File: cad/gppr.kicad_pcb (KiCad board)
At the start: 2 copper layers, 48 x 85 mm, 32 parts, among them J1 Conn_01x04_Female, J2 Conn_01x02_Female, J3 Conn_Coaxial, Q1 IRLR2908, U1 TPS7A470X

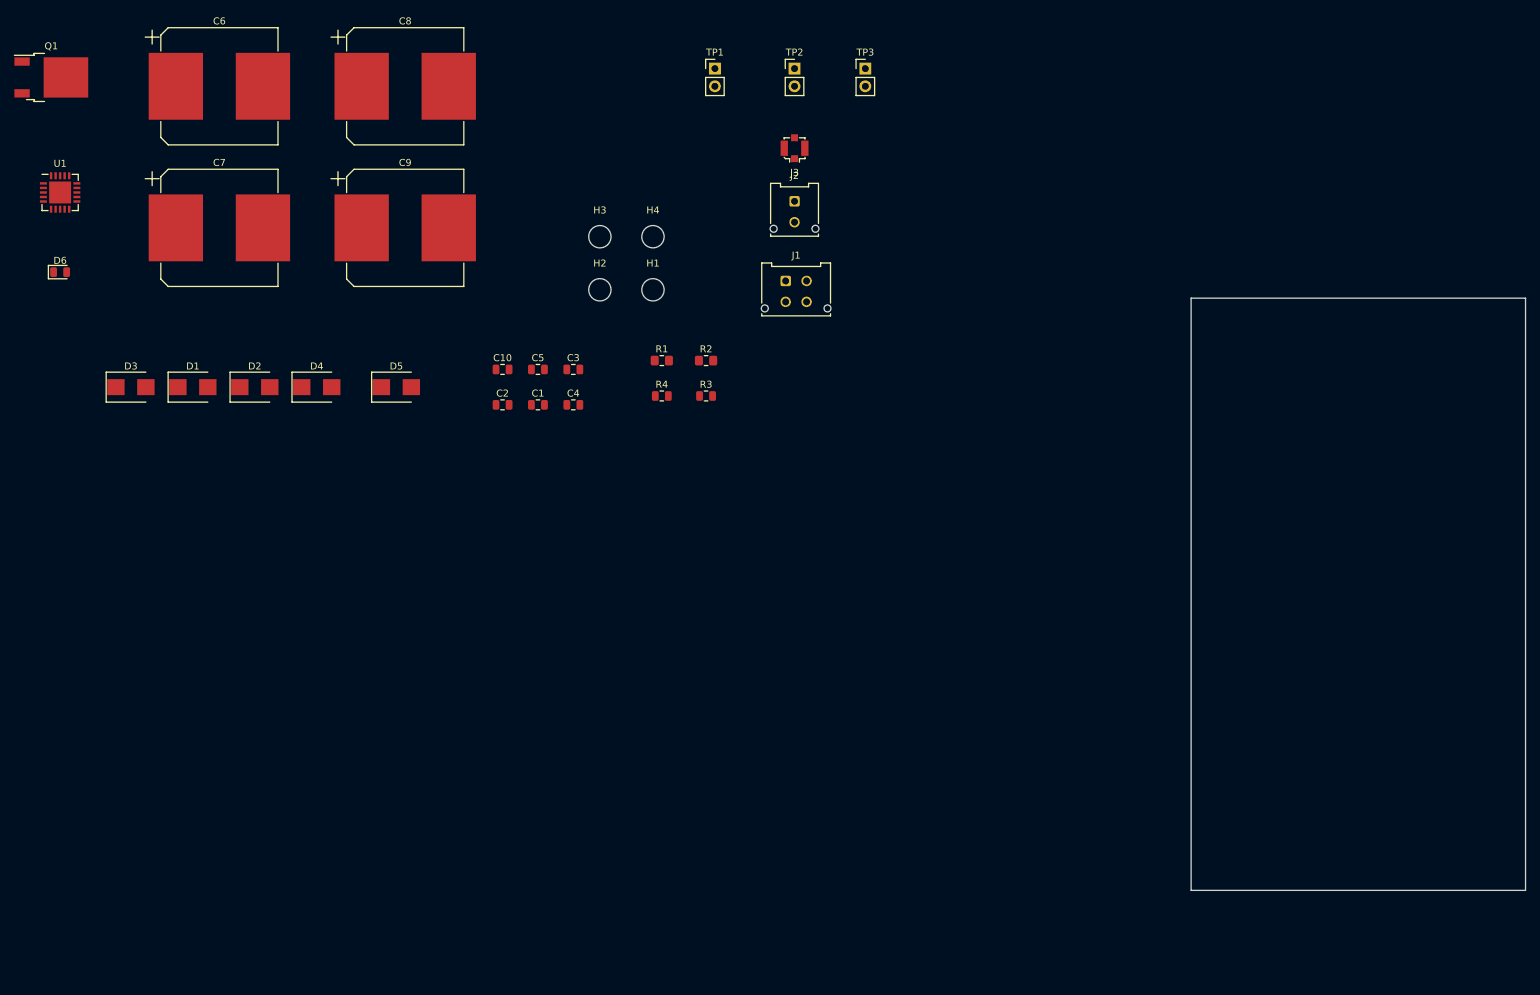
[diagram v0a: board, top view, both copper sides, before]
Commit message: basic component placement, prep for trace routing
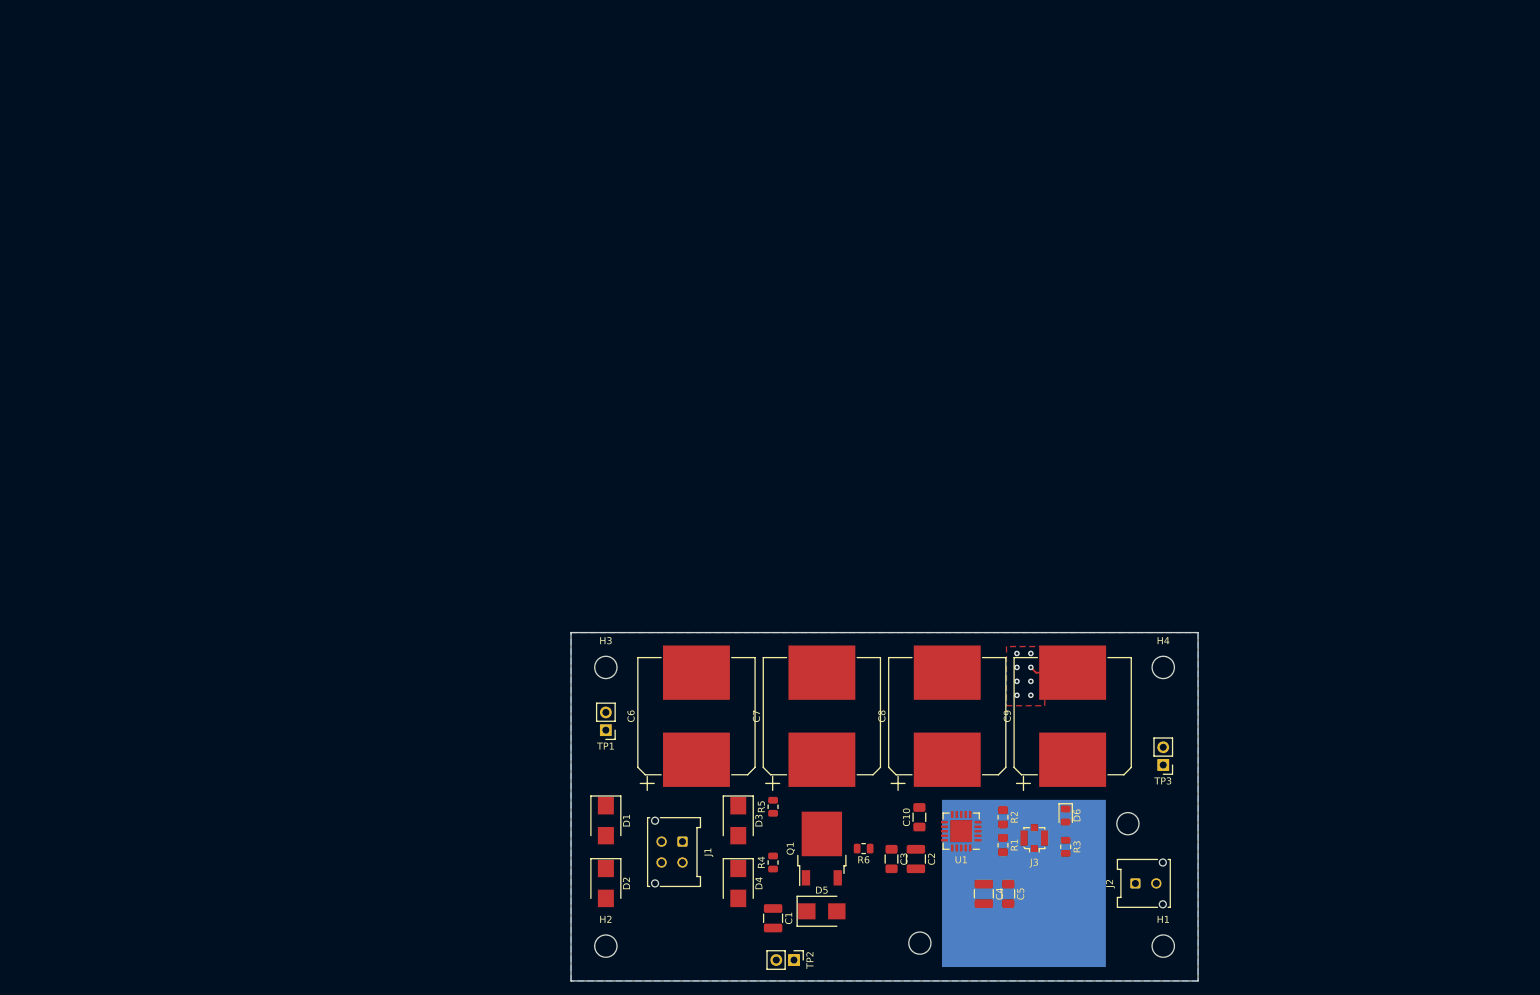
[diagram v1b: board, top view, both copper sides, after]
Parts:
- added HS1: Heatsink_Pad, Heatsink:Heatsink_960-23-XX-F-AB-0, F.Cu at (165.0, 136.0)
- added R5: 0Ω, Resistor_SMD:R_0805_2012Metric, F.Cu at (129.0, 125.0)
- added R6: 0Ω, Resistor_SMD:R_0805_2012Metric, F.Cu at (142.0, 131.0)
- C1, C2, C4: footprint Capacitor_SMD:C_0805_2012Metric -> Capacitor_SMD:C_1210_3225Metric
- C10, C3, C5: footprint Capacitor_SMD:C_0805_2012Metric -> Capacitor_SMD:C_1206_3216Metric
- moved D6 164.1 mm to (171.0, 126.2), turned to 270 degrees
- moved U1 158.5 mm to (156.0, 128.5), turned to 180 degrees
- moved Q1 156.5 mm to (136.0, 131.0), turned to 90 degrees
- moved TP2 128.0 mm to (132.0, 147.0), turned to 270 degrees
- moved H1 119.3 mm to (185.0, 145.0)
- moved C8 119.3 mm to (154.0, 112.0), turned to 90 degrees
- moved C9 118.7 mm to (172.0, 112.0), turned to 90 degrees
- moved C6 113.4 mm to (118.0, 112.0), turned to 90 degrees
- moved C7 111.3 mm to (136.0, 112.0), turned to 90 degrees
- moved J2 109.4 mm to (181.0, 136.0), turned to 90 degrees
- moved TP3 108.7 mm to (185.0, 119.0), turned to 180 degrees
- moved D3 107.1 mm to (124.0, 127.0), turned to 270 degrees
- moved J3 104.8 mm to (166.5, 129.5)
- moved C5 101.1 mm to (162.8, 137.5), turned to 270 degrees
- moved D5 96.9 mm to (136.0, 140.0)
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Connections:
- D5 pad 2: Net-(C2-Pad1) -> Net-(D5-Pad2)
- Q1 pad 2: Net-(C6-Pad1) -> Net-(Q1-Pad2)
- Q1 pad 3: Net-(C2-Pad1) -> Net-(D5-Pad2)
- R4 pad 2: Net-(C6-Pad1) -> Net-(Q1-Pad2)
- TP2 pad 1: Net-(C2-Pad1) -> Net-(D5-Pad2)
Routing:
- net GND: track 0.00 -> 6.31 mm, vias 0 -> 8
- added copper zone on B.Cu, net GND
- added copper zone on F.Cu, net GND
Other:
- board size 48 x 85 mm -> 90 x 50 mm
- net class Default: trace_width 0.25 -> 0.35
- rule pad_to_mask_clearance: 0.051 -> 0

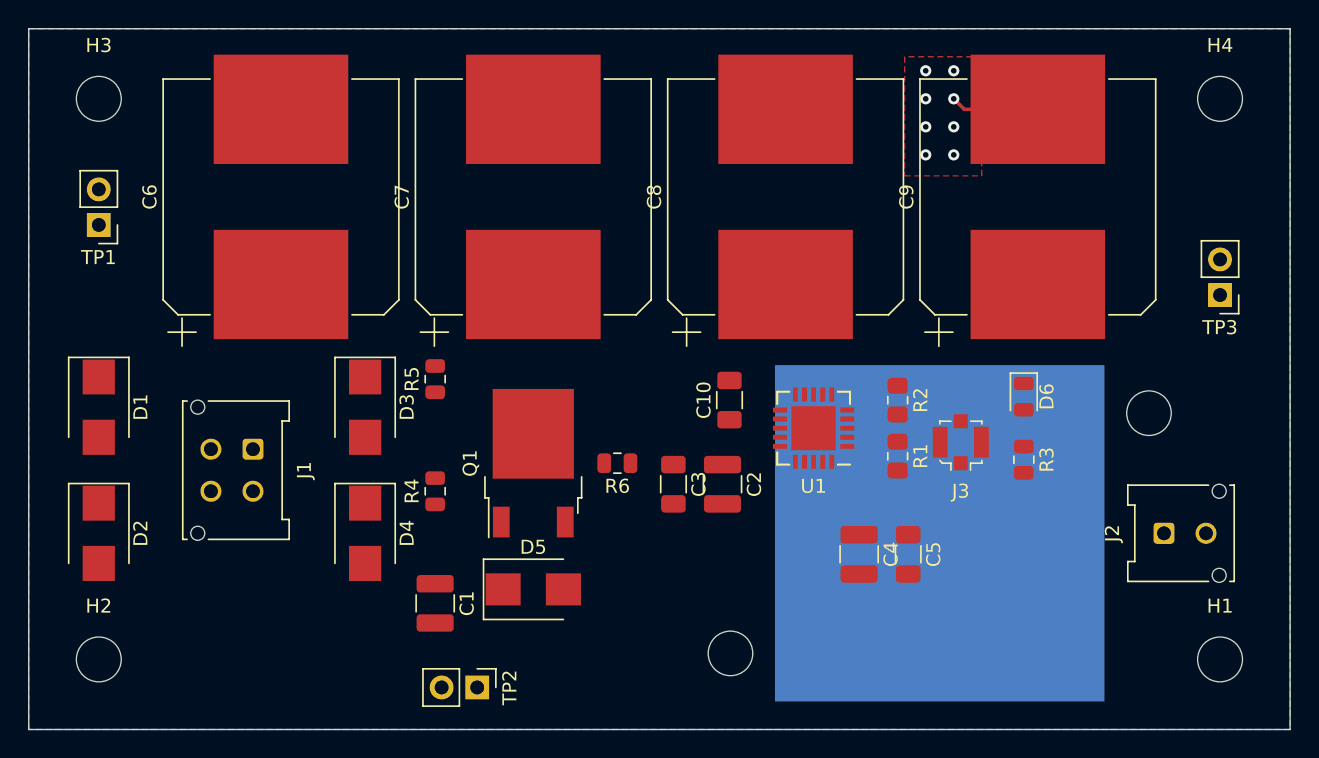
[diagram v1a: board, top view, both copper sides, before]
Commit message: change heatsink footprint from bottom to top side
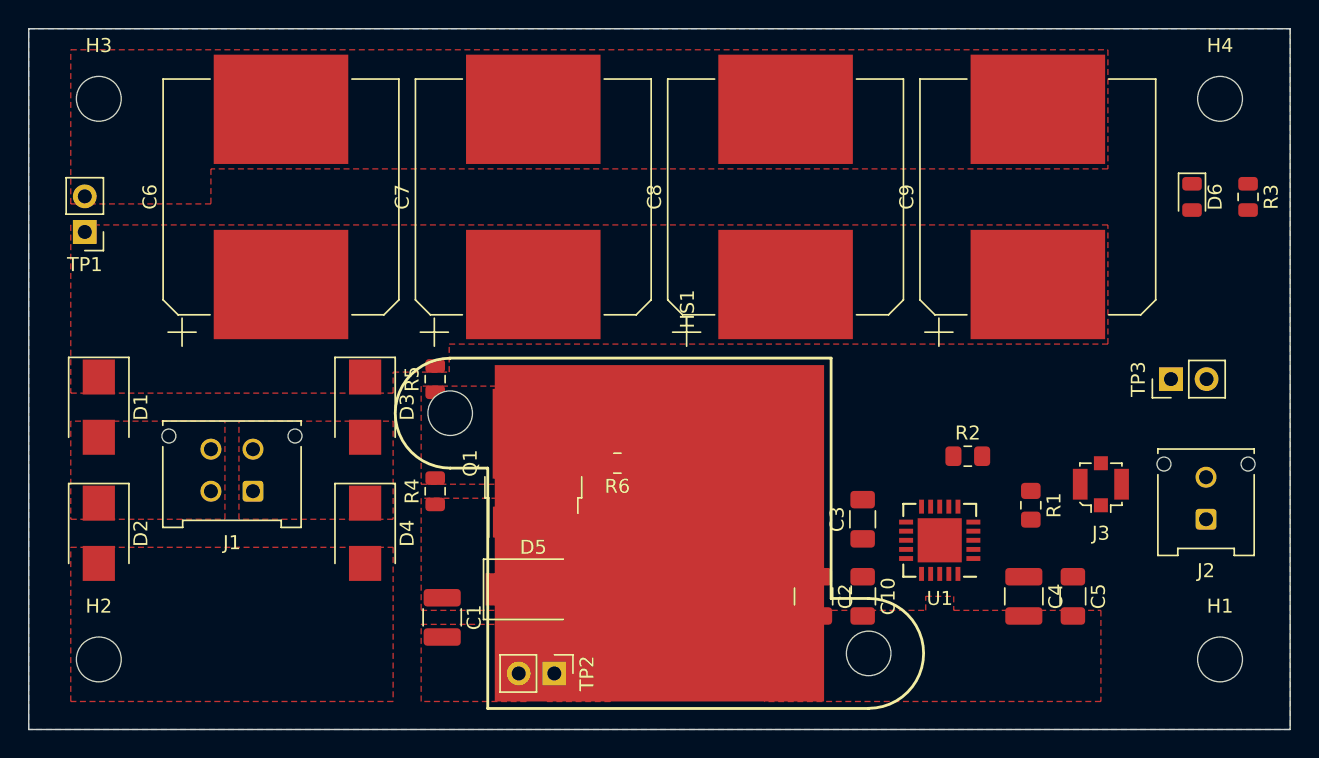
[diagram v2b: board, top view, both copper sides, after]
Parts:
- HS1: footprint Heatsink:Heatsink_960-23-XX-F-AB-0 -> Heatsink:Heatsink_960-23-XX-F-AB-0_Top
- moved R3 24.6 mm to (187.0, 112.0)
- moved HS1 20.0 mm to (145.0, 136.0)
- moved D6 18.6 mm to (183.0, 112.0)
- moved C10 16.9 mm to (159.5, 140.5), turned to 270 degrees
- moved C3 13.7 mm to (159.5, 135.0), turned to 90 degrees
- moved C4 12.1 mm to (171.0, 140.5)
- moved C5 12.1 mm to (174.5, 140.5)
- moved U1 12.0 mm to (165.0, 136.5)
- moved J3 10.4 mm to (176.5, 132.5)
- moved C2 10.3 mm to (156.0, 140.5)
- moved R1 10.1 mm to (171.5, 134.0)
- moved TP3 6.95 mm to (181.5, 125.0), turned to 90 degrees
- moved R2 6.40 mm to (167.0, 130.5), turned to 0 degrees
- moved TP2 5.59 mm to (137.5, 146.0)
- moved J2 3.16 mm to (184.0, 135.0), turned to 180 degrees
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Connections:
- U1 pad 17: Net-(U1-Pad17) -> GND
- U1 pad 18: Net-(U1-Pad18) -> GND
- U1 pad 19: Net-(U1-Pad19) -> GND
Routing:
- net GND: track 6.31 -> 0.00 mm, vias 8 -> 0
- added copper zone on F.Cu, net Net-(C1-Pad1)
- added copper zone on F.Cu, net Net-(C6-Pad1)
- added copper zone on F.Cu, net Net-(D1-Pad2)
- added copper zone on F.Cu, net Net-(D3-Pad2)
- added copper zone on F.Cu, net Net-(D5-Pad2)
- added copper zone on F.Cu, net Net-(Q1-Pad2)

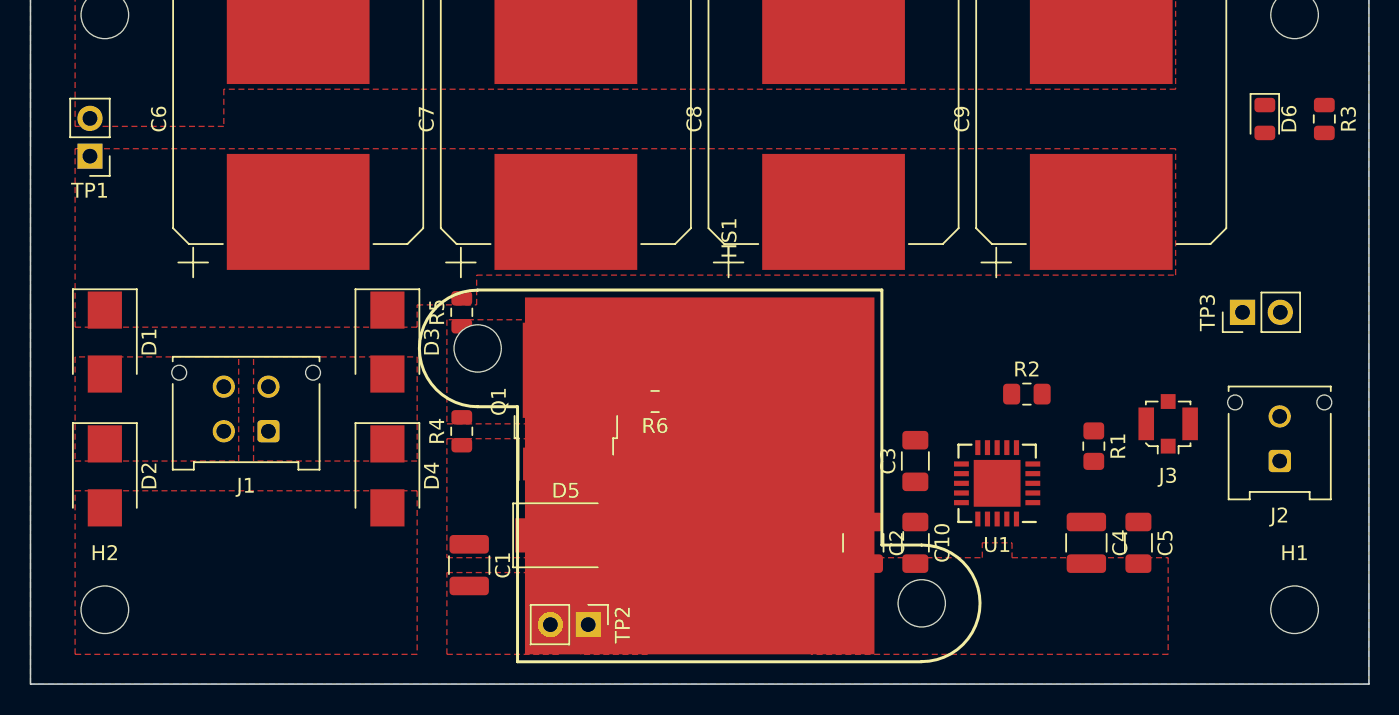
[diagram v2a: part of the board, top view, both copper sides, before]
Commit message: reposition components, prep to route
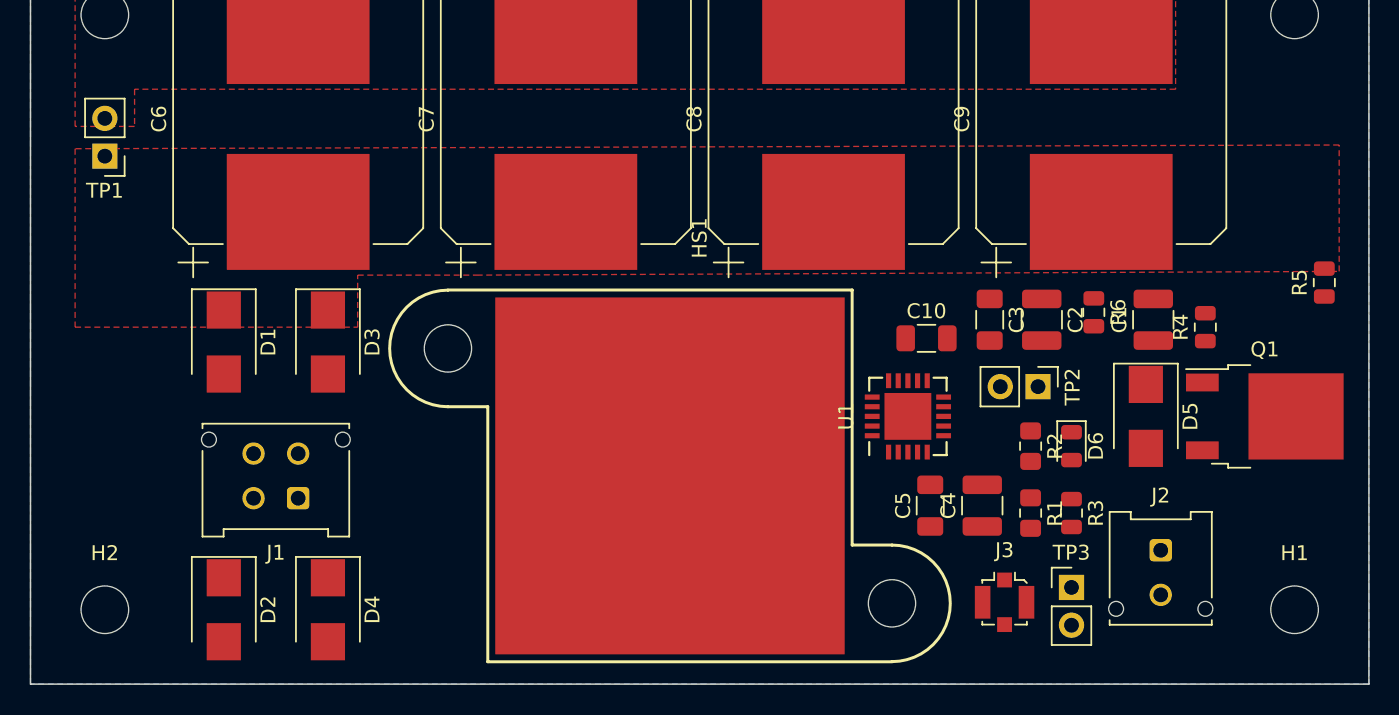
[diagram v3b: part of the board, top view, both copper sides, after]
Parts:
- moved R5 58.0 mm to (187.0, 123.0)
- moved R4 50.5 mm to (179.0, 126.0)
- moved C1 48.9 mm to (175.5, 125.5), turned to 90 degrees
- moved Q1 47.0 mm to (183.0, 132.0), turned to 0 degrees
- moved D5 39.8 mm to (175.0, 132.0), turned to 270 degrees
- moved TP2 34.2 mm to (167.8, 130.0)
- moved R3 31.5 mm to (170.0, 138.5)
- moved R6 30.1 mm to (171.5, 125.0), turned to 270 degrees
- moved D6 25.6 mm to (170.0, 134.0)
- moved TP3 21.8 mm to (170.0, 143.5), turned to 0 degrees
- moved C2 19.2 mm to (168.0, 125.5)
- moved J3 16.3 mm to (165.5, 144.5), turned to 180 degrees
- moved C5 14.2 mm to (160.5, 138.0), turned to 90 degrees
- moved C10 13.8 mm to (160.2, 126.8), turned to 0 degrees
- moved D2 12.0 mm to (113.0, 145.0)
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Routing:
- removed copper zone on F.Cu, net Net-(C1-Pad1)
- removed copper zone on F.Cu, net Net-(D1-Pad2)
- removed copper zone on F.Cu, net Net-(D3-Pad2)
- removed copper zone on F.Cu, net Net-(D5-Pad2)
- removed copper zone on F.Cu, net Net-(Q1-Pad2)

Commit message: route the board
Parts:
- moved TP1 79.5 mm to (184.5, 115.0)
- moved D3 17.0 mm to (108.0, 115.0)
- moved D1 15.3 mm to (103.5, 115.0)
- moved D4 15.0 mm to (108.0, 136.0)
- moved J1 14.1 mm to (108.0, 127.5)
- moved C2 13.8 mm to (154.5, 128.5), turned to 180 degrees
- moved D2 13.1 mm to (103.5, 136.0)
- moved R6 11.5 mm to (160.0, 125.0), turned to 0 degrees
- moved HS1 11.0 mm to (132.0, 136.0)
- moved C4 10.5 mm to (154.5, 142.5), turned to 180 degrees
- moved C3 10.0 mm to (154.5, 125.0), turned to 180 degrees
- moved Q1 9.55 mm to (173.5, 133.0), turned to 270 degrees
- moved R5 7.81 mm to (182.0, 117.0)
- moved D5 7.16 mm to (173.5, 125.0), turned to 180 degrees
- moved C5 6.08 mm to (154.5, 139.0), turned to 180 degrees
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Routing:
- net Net-(R1-Pad1): track 0.00 -> 9.77 mm
- net Net-(C2-Pad1): track 0.00 -> 8.20 mm
- net Net-(C10-Pad1): track 0.00 -> 3.41 mm
- net Net-(D6-Pad2): track 0.00 -> 3.12 mm
- net Net-(Q1-Pad2): vias 0 -> 17
- net GND: vias 0 -> 48
- added copper zone on F.Cu, net Net-(C1-Pad1)
- added copper zone on F.Cu, net Net-(C2-Pad1)
- added copper zone on F.Cu, net Net-(C4-Pad1)
- added copper zone on F.Cu, net Net-(D1-Pad2)
- added copper zone on F.Cu, net Net-(D3-Pad2)
- added copper zone on F.Cu, net Net-(D5-Pad2)
- added copper zone on B.Cu, net Net-(Q1-Pad2)
- added copper zone on F.Cu, net Net-(Q1-Pad2)
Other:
- net class Default: trace_width 0.35 -> 0.3; via_dia 0.8 -> 1
- net class power added: clearance 0.2, trace_width 1, via_dia 1, via_drill 0.4
- board text added: "(C) 2019"
- board text added: "GPPR v0.1"
- board text added: "Gosselin"
- board text added: "Michael"
- board text added: "github.com/mgosselin/gppr"
